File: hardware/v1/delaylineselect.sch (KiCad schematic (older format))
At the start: 4 parts, among them P1 CONN_02X02, SW1 SW_PUSH, SW2 Coded_Switch, U1 MCP23017

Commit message: Simplify routing for delaylineselect, generate gerber files and svg.
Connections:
- wire segments 22 -> 24
- no-connect marks 15 -> 14
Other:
- moved on the sheet: SW1
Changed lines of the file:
@@
 LIBS:contrib
 LIBS:valves
-LIBS:MAX7221
-LIBS:MCP23S17
-LIBS:MCP23017
-LIBS:Pi2_Connector
 LIBS:delaylineselect-cache
 EELAYER 25 0
@@
 	1    0    0    -1
 $EndComp
-Wire Wire Line
-	4200 2000 3050 2000
-Wire Wire Line
-	3050 2100 4200 2100
-Wire Wire Line
-	4200 2200 3050 2200
-Wire Wire Line
-	3050 2300 4200 2300
-Text Label 3050 2300 0    60   ~ 0
+Text Label 3300 2300 0    60   ~ 0
 SELECT_A
 Text Label 4200 2500 0    60   ~ 0
 E
-Text Label 3050 2200 0    60   ~ 0
+Text Label 3300 2200 0    60   ~ 0
 SELECT_B
-Text Label 3050 2100 0    60   ~ 0
+Text Label 3300 2100 0    60   ~ 0
 SELECT_C
-Text Label 3050 2000 0    60   ~ 0
+Text Label 3300 2000 0    60   ~ 0
 SELECT_D
-NoConn ~ 1550 1600
 NoConn ~ 3050 1700
 NoConn ~ 3050 1800
@@
 	1    0    0    -1
 $EndComp
-Wire Wire Line
-	4200 2500 4200 2600
 NoConn ~ 1550 2600
 NoConn ~ 1550 2900
@@
 	1    0    0    -1
 $EndComp
-Wire Wire Line
-	1850 3750 2150 3750
-Wire Wire Line
-	2150 3750 2150 3900
-Wire Wire Line
-	2150 4000 1650 4000
-Wire Wire Line
-	1650 4000 1650 3850
 Text Label 1550 2800 2    60   ~ 0
 SDA
@@
 Text Label 1550 2700 2    60   ~ 0
 SCK
-Wire Wire Line
-	1200 2400 1550 2400
-Wire Wire Line
-	1550 2500 1200 2500
-Wire Wire Line
-	1200 2500 1200 2550
 NoConn ~ 3050 2400
 NoConn ~ 3050 2500
@@
 	1    0    0    -1
 $EndComp
-Wire Wire Line
-	3250 2600 3050 2600
 $Comp
 L GND #PWR07
@@
 Text Notes 2700 3250 0    60   ~ 0
 ADDR 010\n
-Wire Wire Line
-	3050 2800 3250 2800
-Wire Wire Line
-	3250 2800 3250 2600
-Wire Wire Line
-	3050 2700 3150 2700
-Wire Wire Line
-	3150 2700 3150 2900
-Wire Wire Line
-	3050 2900 3250 2900
-Wire Wire Line
-	3250 2900 3250 3000
-Connection ~ 3150 2900
 $Comp
 L SW_PUSH SW1
 U 1 1 57A8BC2B
-P 4800 1600
-F 0 "SW1" H 4950 1710 50  0000 C CNN
-F 1 "SW_PUSH" H 4800 1520 50  0000 C CNN
-F 2 "Buttons_Switches_ThroughHole:SW_PUSH" H 4800 1600 50  0001 C CNN
-F 3 "" H 4800 1600 50  0000 C CNN
-	1    4800 1600
-	1    0    0    -1
-$EndComp
-Wire Wire Line
-	4500 1600 3050 1600
-Wire Wire Line
-	5100 1600 5250 1600
-Wire Wire Line
-	5250 1600 5250 1750
+P 2375 975
+F 0 "SW1" H 2525 1085 50  0000 C CNN
+F 1 "SW_PUSH" H 2375 895 50  0000 C CNN
+F 2 "Buttons_Switches_ThroughHole:SW_PUSH" H 2375 975 50  0001 C CNN
+F 3 "" H 2375 975 50  0000 C CNN
+	1    2375 975
+	1    0    0    -1
+$EndComp
 $Comp
 L GND #PWR08
 U 1 1 57A8BCDC
-P 5250 1750
-F 0 "#PWR08" H 5250 1500 50  0001 C CNN
-F 1 "GND" H 5250 1600 50  0000 C CNN
-F 2 "" H 5250 1750 50  0000 C CNN
-F 3 "" H 5250 1750 50  0000 C CNN
-	1    5250 1750
-	1    0    0    -1
-$EndComp
-Text Label 3050 1600 0    60   ~ 0
+P 2825 1125
+F 0 "#PWR08" H 2825 875 50  0001 C CNN
+F 1 "GND" H 2825 975 50  0000 C CNN
+F 2 "" H 2825 1125 50  0000 C CNN
+F 3 "" H 2825 1125 50  0000 C CNN
+	1    2825 1125
+	1    0    0    -1
+$EndComp
+Text Label 1425 975  0    60   ~ 0
 MCSLIP
 Text Label 2650 4000 0    60   ~ 0
 SDA
+Wire Wire Line
+	4200 2000 3050 2000
+Wire Wire Line
+	3050 2100 4200 2100
+Wire Wire Line
+	4200 2200 3050 2200
+Wire Wire Line
+	3050 2300 4200 2300
+Wire Wire Line
+	4200 2500 4200 2600
+Wire Wire Line
+	1850 3750 2150 3750
+Wire Wire Line
+	2150 3750 2150 3900
+Wire Wire Line
+	2150 4000 1650 4000
+Wire Wire Line
+	1650 4000 1650 3850
+Wire Wire Line
+	1200 2400 1550 2400
+Wire Wire Line
+	1550 2500 1200 2500
+Wire Wire Line
+	1200 2500 1200 2550
+Wire Wire Line
+	3250 2600 3050 2600
+Wire Wire Line
+	3050 2800 3250 2800
+Wire Wire Line
+	3250 2800 3250 2600
+Wire Wire Line
+	3050 2700 3150 2700
+Wire Wire Line
+	3150 2700 3150 2900
+Wire Wire Line
+	3050 2900 3250 2900
+Wire Wire Line
+	3250 2900 3250 3000
+Connection ~ 3150 2900
+Wire Wire Line
+	2675 975  2825 975
+Wire Wire Line
+	2825 975  2825 1125
+Wire Wire Line
+	1425 1600 1550 1600
+Wire Wire Line
+	1425 975  1425 1600
+Wire Wire Line
+	1425 975  2075 975
 $EndSCHEMATC

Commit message: Re-arrange switch connector pinout to simpler single-row header. Re-route the switch boards accordingly.
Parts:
- removed P1: CONN_02X02, Pin_Headers:Pin_Header_Angled_2x02, symbol CONN_02X02
- added P1: CONN_01X04, Pin_Headers:Pin_Header_Angled_1x04, symbol CONN_01X04
- SW1: footprint Buttons_Switches_ThroughHole:SW_PUSH -> Pin_Headers:Pin_Header_Straight_2x01
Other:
- note removed: "ADDR 010\n"
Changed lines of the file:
@@
 LIBS:contrib
 LIBS:valves
+LIBS:MAX7221
+LIBS:MCP23S17
+LIBS:MCP23017
+LIBS:Pi2_Connector
 LIBS:delaylineselect-cache
 EELAYER 25 0
@@
 NoConn ~ 1550 2900
 $Comp
-L CONN_02X02 P1
-U 1 1 57A8B1C9
-P 2400 3950
-F 0 "P1" H 2400 4100 50  0000 C CNN
-F 1 "CONN_02X02" H 2400 3800 50  0000 C CNN
-F 2 "Pin_Headers:Pin_Header_Angled_2x02" H 2400 2750 50  0001 C CNN
-F 3 "" H 2400 2750 50  0000 C CNN
-	1    2400 3950
-	1    0    0    -1
-$EndComp
-$Comp
 L VDD #PWR04
 U 1 1 57A8B1D0
-P 1650 3850
-F 0 "#PWR04" H 1650 3700 50  0001 C CNN
-F 1 "VDD" H 1650 4000 50  0000 C CNN
-F 2 "" H 1650 3850 50  0000 C CNN
-F 3 "" H 1650 3850 50  0000 C CNN
-	1    1650 3850
+P 1850 4300
+F 0 "#PWR04" H 1850 4150 50  0001 C CNN
+F 1 "VDD" H 1850 4450 50  0000 C CNN
+F 2 "" H 1850 4300 50  0000 C CNN
+F 3 "" H 1850 4300 50  0000 C CNN
+	1    1850 4300
 	1    0    0    -1
 $EndComp
@@
 L GND #PWR05
 U 1 1 57A8B1D6
-P 1850 3750
-F 0 "#PWR05" H 1850 3500 50  0001 C CNN
-F 1 "GND" H 1850 3600 50  0000 C CNN
-F 2 "" H 1850 3750 50  0000 C CNN
-F 3 "" H 1850 3750 50  0000 C CNN
-	1    1850 3750
+P 2050 4150
+F 0 "#PWR05" H 2050 3900 50  0001 C CNN
+F 1 "GND" H 2050 4000 50  0000 C CNN
+F 2 "" H 2050 4150 50  0000 C CNN
+F 3 "" H 2050 4150 50  0000 C CNN
+	1    2050 4150
 	1    0    0    -1
 $EndComp
 Text Label 1550 2800 2    60   ~ 0
 SDA
-Text Label 2650 3900 0    60   ~ 0
+Text Label 2250 4650 2    60   ~ 0
 SCK
 Text Label 1550 2700 2    60   ~ 0
@@
 	1    0    0    -1
 $EndComp
-Text Notes 2700 3250 0    60   ~ 0
-ADDR 010\n
 $Comp
 L SW_PUSH SW1
@@
 F 0 "SW1" H 2525 1085 50  0000 C CNN
 F 1 "SW_PUSH" H 2375 895 50  0000 C CNN
-F 2 "Buttons_Switches_ThroughHole:SW_PUSH" H 2375 975 50  0001 C CNN
+F 2 "Pin_Headers:Pin_Header_Straight_2x01" H 2375 975 50  0001 C CNN
 F 3 "" H 2375 975 50  0000 C CNN
 	1    2375 975
@@
 Text Label 1425 975  0    60   ~ 0
 MCSLIP
-Text Label 2650 4000 0    60   ~ 0
+Text Label 2250 4550 2    60   ~ 0
 SDA
 Wire Wire Line
@@
 Wire Wire Line
 	4200 2500 4200 2600
-Wire Wire Line
-	1850 3750 2150 3750
-Wire Wire Line
-	2150 3750 2150 3900
-Wire Wire Line
-	2150 4000 1650 4000
-Wire Wire Line
-	1650 4000 1650 3850
 Wire Wire Line
 	1200 2400 1550 2400
@@
 Wire Wire Line
 	1425 975  2075 975
+$Comp
+L CONN_01X04 P1
+U 1 1 57A9BE7E
+P 2450 4500
+F 0 "P1" H 2450 4750 50  0000 C CNN
+F 1 "CONN_01X04" V 2550 4500 50  0000 C CNN
+F 2 "Pin_Headers:Pin_Header_Angled_1x04" H 2450 4500 50  0001 C CNN
+F 3 "" H 2450 4500 50  0000 C CNN
+	1    2450 4500
+	1    0    0    -1
+$EndComp
+Wire Wire Line
+	2050 4150 2250 4150
+Wire Wire Line
+	2250 4150 2250 4350
+Wire Wire Line
+	2250 4450 1850 4450
+Wire Wire Line
+	1850 4450 1850 4300
 $EndSCHEMATC

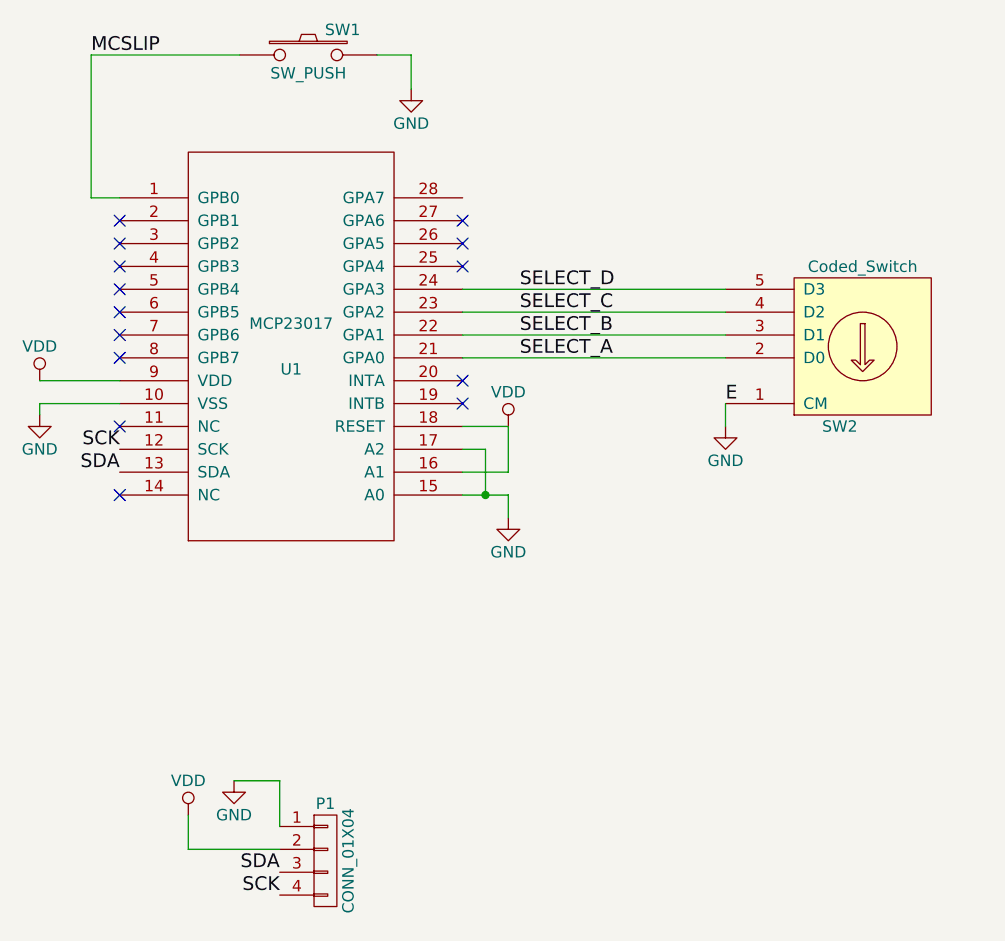
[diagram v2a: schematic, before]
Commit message: Add new schematics for additional switch boards
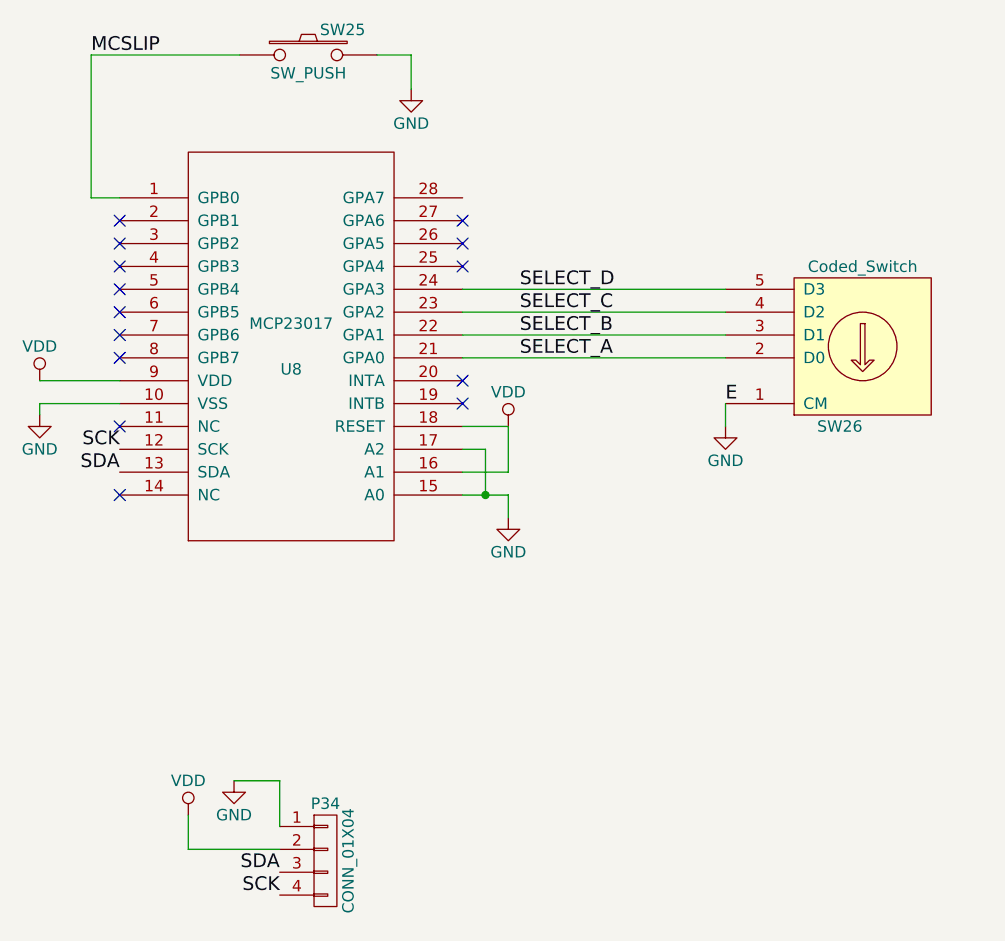
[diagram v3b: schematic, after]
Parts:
- renumbered P1 to P34, SW1 to SW25, SW2 to SW26, U1 to U8
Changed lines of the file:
@@
 LIBS:MCP23017
 LIBS:Pi2_Connector
-LIBS:delaylineselect-cache
+LIBS:v1-cache
 EELAYER 25 0
 EELAYER END
 $Descr A4 11693 8268
 encoding utf-8
-Sheet 1 1
+Sheet 1 30
 Title ""
 Date ""
@@
 $EndDescr
 $Comp
-L Coded_Switch SW2
+L Coded_Switch SW26
 U 1 1 57A8A7D6
 P 4800 2250
-F 0 "SW2" H 4900 2600 50  0000 C CNN
+F 0 "SW26" H 4900 2600 50  0000 C CNN
 F 1 "Coded_Switch" H 4800 1901 50  0000 C CNN
 F 2 "myparts:ROTARY_BCK1002-custom" H 4800 2250 50  0001 C CNN
@@
 $EndComp
 $Comp
-L MCP23017 U1
+L MCP23017 U8
 U 1 1 57A8A9AF
 P 2300 2250
-F 0 "U1" H 2300 2150 50  0000 C CNN
+F 0 "U8" H 2300 2150 50  0000 C CNN
 F 1 "MCP23017" H 2300 2350 50  0000 C CNN
 F 2 "DIL28:DIL28" H 2300 2250 50  0001 C CNN
@@
 NoConn ~ 1550 2300
 $Comp
-L VDD #PWR01
+L VDD #PWR36
 U 1 1 57A8ABB1
 P 1200 2400
-F 0 "#PWR01" H 1200 2250 50  0001 C CNN
+F 0 "#PWR36" H 1200 2250 50  0001 C CNN
 F 1 "VDD" H 1200 2550 50  0000 C CNN
 F 2 "" H 1200 2400 50  0000 C CNN
@@
 $EndComp
 $Comp
-L GND #PWR02
+L GND #PWR37
 U 1 1 57A8ABCB
 P 1200 2550
-F 0 "#PWR02" H 1200 2300 50  0001 C CNN
+F 0 "#PWR37" H 1200 2300 50  0001 C CNN
 F 1 "GND" H 1200 2400 50  0000 C CNN
 F 2 "" H 1200 2550 50  0000 C CNN
@@
 $EndComp
 $Comp
-L GND #PWR03
+L GND #PWR43
 U 1 1 57A8ABF5
 P 4200 2600
-F 0 "#PWR03" H 4200 2350 50  0001 C CNN
+F 0 "#PWR43" H 4200 2350 50  0001 C CNN
 F 1 "GND" H 4200 2450 50  0000 C CNN
 F 2 "" H 4200 2600 50  0000 C CNN
@@
 NoConn ~ 1550 2900
 $Comp
-L VDD #PWR04
+L VDD #PWR38
 U 1 1 57A8B1D0
 P 1850 4300
-F 0 "#PWR04" H 1850 4150 50  0001 C CNN
+F 0 "#PWR38" H 1850 4150 50  0001 C CNN
 F 1 "VDD" H 1850 4450 50  0000 C CNN
 F 2 "" H 1850 4300 50  0000 C CNN
@@
 $EndComp
 $Comp
-L GND #PWR05
+L GND #PWR39
 U 1 1 57A8B1D6
 P 2050 4150
-F 0 "#PWR05" H 2050 3900 50  0001 C CNN
+F 0 "#PWR39" H 2050 3900 50  0001 C CNN
 F 1 "GND" H 2050 4000 50  0000 C CNN
 F 2 "" H 2050 4150 50  0000 C CNN
@@
 NoConn ~ 3050 2500
 $Comp
-L VDD #PWR06
+L VDD #PWR41
 U 1 1 57A8B7E3
 P 3250 2600
-F 0 "#PWR06" H 3250 2450 50  0001 C CNN
+F 0 "#PWR41" H 3250 2450 50  0001 C CNN
 F 1 "VDD" H 3250 2750 50  0000 C CNN
 F 2 "" H 3250 2600 50  0000 C CNN
@@
 $EndComp
 $Comp
-L GND #PWR07
+L GND #PWR42
 U 1 1 57A8B81A
 P 3250 3000
-F 0 "#PWR07" H 3250 2750 50  0001 C CNN
+F 0 "#PWR42" H 3250 2750 50  0001 C CNN
 F 1 "GND" H 3250 2850 50  0000 C CNN
 F 2 "" H 3250 3000 50  0000 C CNN
@@
 $EndComp
 $Comp
-L SW_PUSH SW1
+L SW_PUSH SW25
 U 1 1 57A8BC2B
 P 2375 975
-F 0 "SW1" H 2525 1085 50  0000 C CNN
+F 0 "SW25" H 2525 1085 50  0000 C CNN
 F 1 "SW_PUSH" H 2375 895 50  0000 C CNN
 F 2 "Pin_Headers:Pin_Header_Straight_2x01" H 2375 975 50  0001 C CNN
@@
 $EndComp
 $Comp
-L GND #PWR08
+L GND #PWR40
 U 1 1 57A8BCDC
 P 2825 1125
-F 0 "#PWR08" H 2825 875 50  0001 C CNN
+F 0 "#PWR40" H 2825 875 50  0001 C CNN
 F 1 "GND" H 2825 975 50  0000 C CNN
 F 2 "" H 2825 1125 50  0000 C CNN
@@
 	1425 975  2075 975
 $Comp
-L CONN_01X04 P1
+L CONN_01X04 P34
 U 1 1 57A9BE7E
 P 2450 4500
-F 0 "P1" H 2450 4750 50  0000 C CNN
+F 0 "P34" H 2450 4750 50  0000 C CNN
 F 1 "CONN_01X04" V 2550 4500 50  0000 C CNN
 F 2 "Pin_Headers:Pin_Header_Angled_1x04" H 2450 4500 50  0001 C CNN
